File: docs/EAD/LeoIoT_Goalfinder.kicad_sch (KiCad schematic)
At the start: 16 parts, among them J1 USB_B_Micro_Breakout, J1e1 Conn_01x02_Pin, J2 LED Strip, J3 GAIN, Q1 IRFZ44N, U1 ESP32_D1_mini, U2 VL53L0X_Breakout, U3 MAX98357A_Breakout, U4 SW420_Breakout, U5 LIS3DH_Breakout

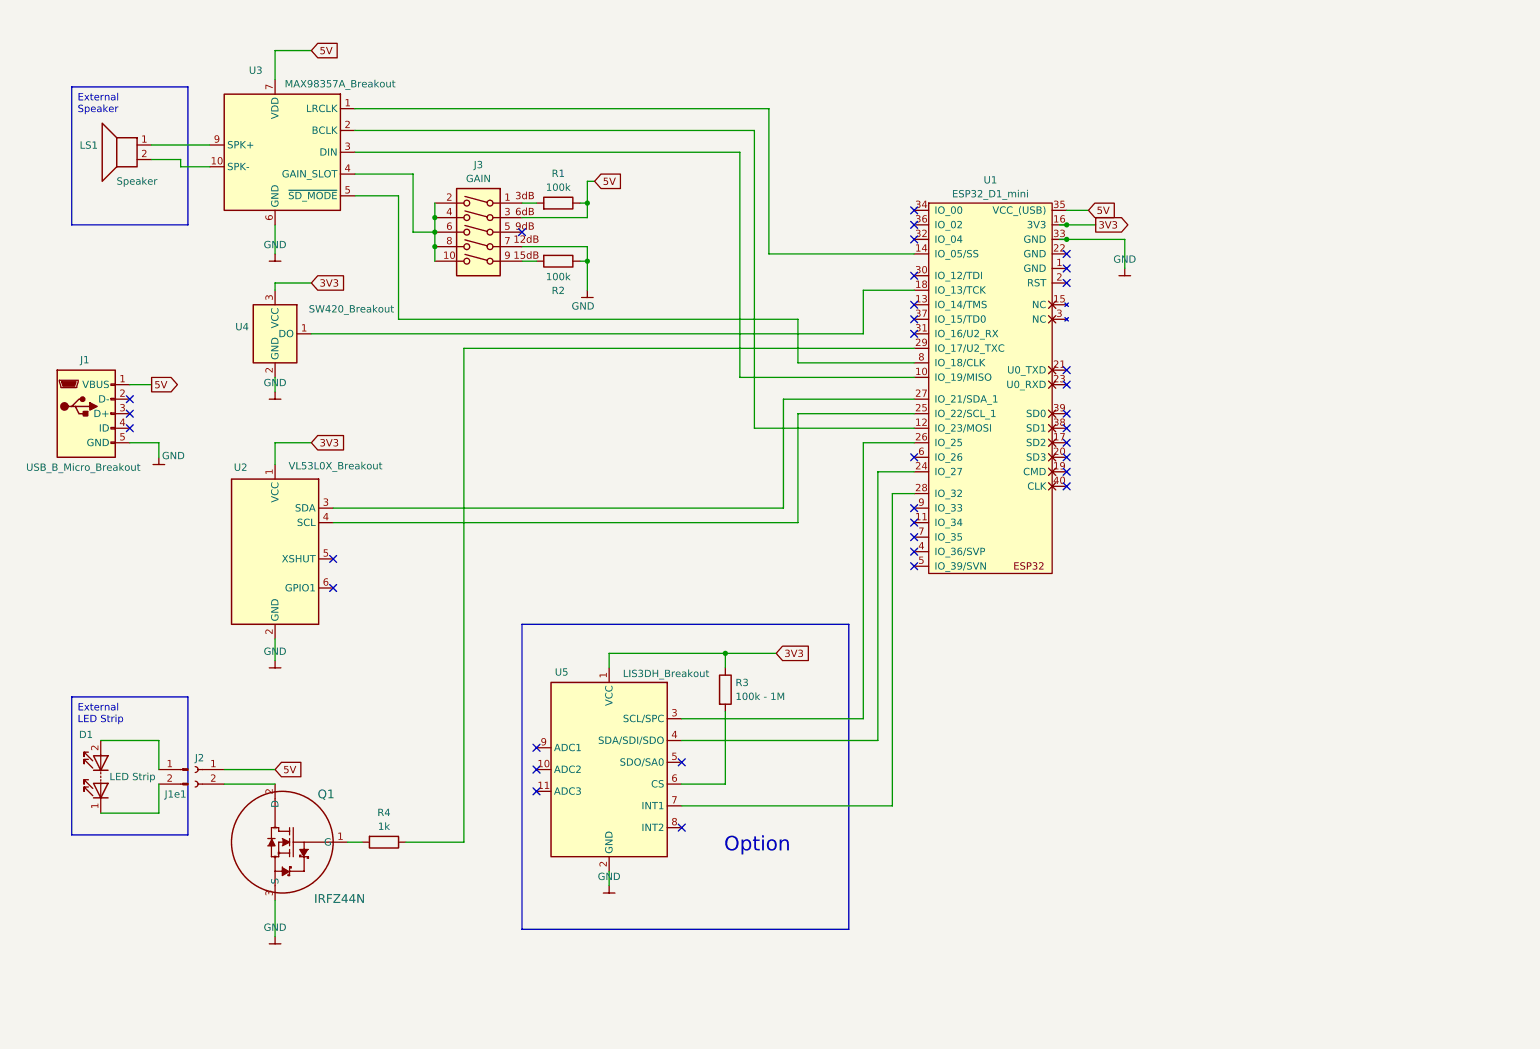
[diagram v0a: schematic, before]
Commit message: added power support capacities, updated schematic and PCB to r1.1
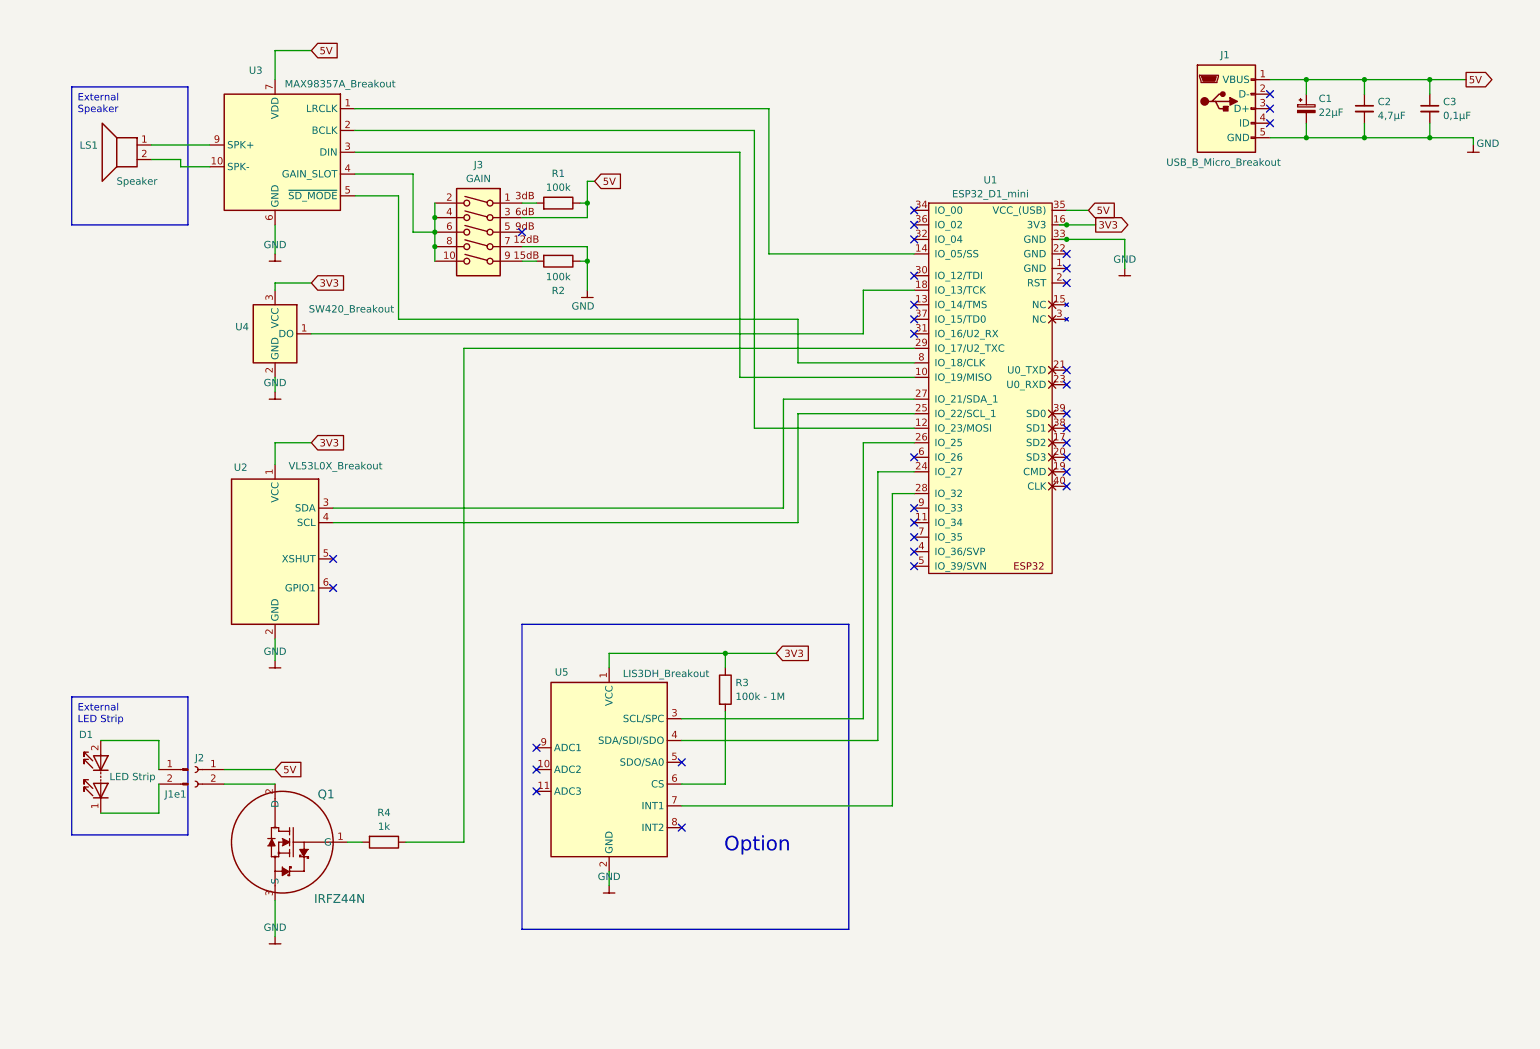
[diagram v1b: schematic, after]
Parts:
- added C1: 22µF, Capacitor_THT:CP_Radial_D5.0mm_P2.00mm, symbol Device:C_Polarized_Small
- added C2: 4,7µF, Capacitor_THT:CP_Radial_D5.0mm_P2.00mm, symbol Device:C_Small
- added C3: 0,1µF, Capacitor_THT:C_Rect_L13.0mm_W4.0mm_P10.00mm_FKS3_FKP3_MKS4, symbol Device:C_Small
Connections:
- net 5V: now also C1.1, C2.1, C3.1
- net GND: now also C1.2, C2.2, C3.2
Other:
- moved on the sheet: J1

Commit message: improved HW: - added capacitors for each breakout board - made GND lines wider and added GND shield areas - added HW revision 01.02 added technical drawings for case factoring
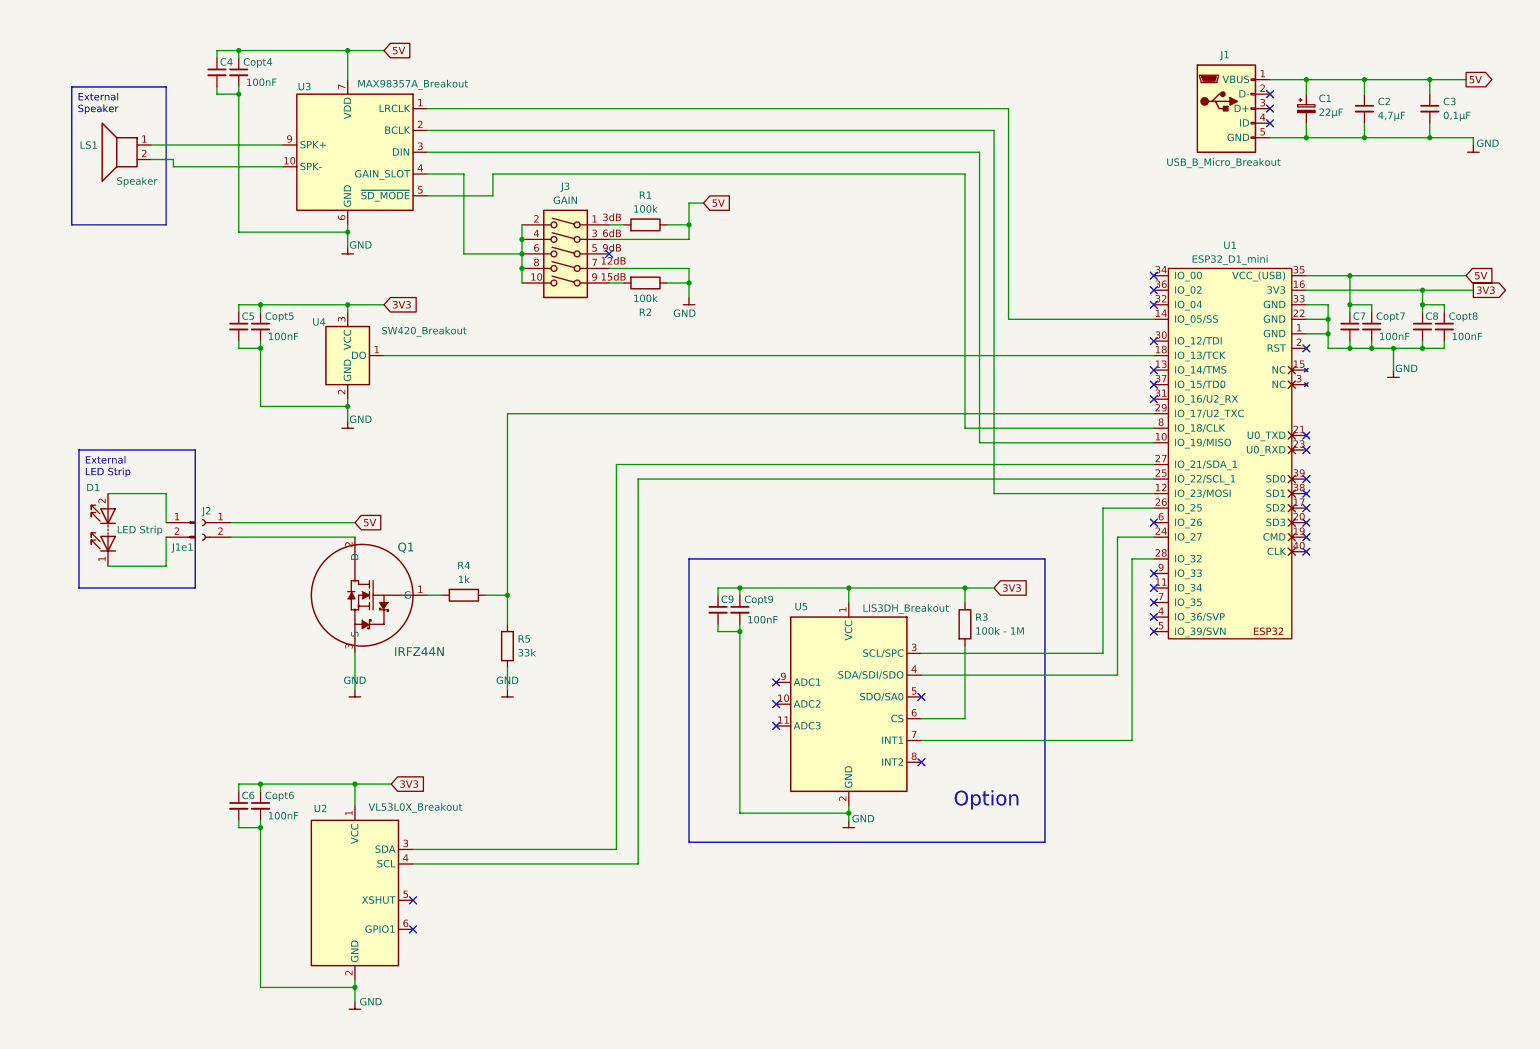
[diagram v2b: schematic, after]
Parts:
- added C4, C5, C6, C7, C8, C9: 100nF, Capacitor_SMD:C_0805_2012Metric_Pad1.18x1.45mm_HandSolder, symbol Device:C_Small
- added Copt4, Copt5, Copt6, Copt7, Copt8, Copt9: 100nF, Capacitor_THT:C_Disc_D5.0mm_W2.5mm_P2.50mm, symbol Device:C_Small
- added R5: 33k, Resistor_THT:R_Axial_DIN0309_L9.0mm_D3.2mm_P12.70mm_Horizontal, symbol Device:R
- R3, U5: now left out of the parts list
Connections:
- net 3V3: now also C5.1, C6.1, C8.1, C9.1, Copt5.1, Copt6.1, Copt8.1, Copt9.1
- net 5V: now also C4.1, C7.1, Copt4.1, Copt7.1
- net GND: now also U1.1 (GND), U1.22 (GND), C4.2, C5.2, C6.2, C7.2, C8.2, C9.2, Copt4.2, Copt5.2, Copt6.2, Copt7.2, Copt8.2, Copt9.2, R5.2
- net at R4.1, U1.29 (IO_17/U2_TXC): now also R5.1
- no-connect marks 35 -> 33
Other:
- moved on the sheet: D1, J1e1, J2, J3, Q1, R1, R2, R3, R4, U1, U2, U3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

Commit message: Refined design and PCB layout and added BOM - added SMD resistors - shaped PCB prints
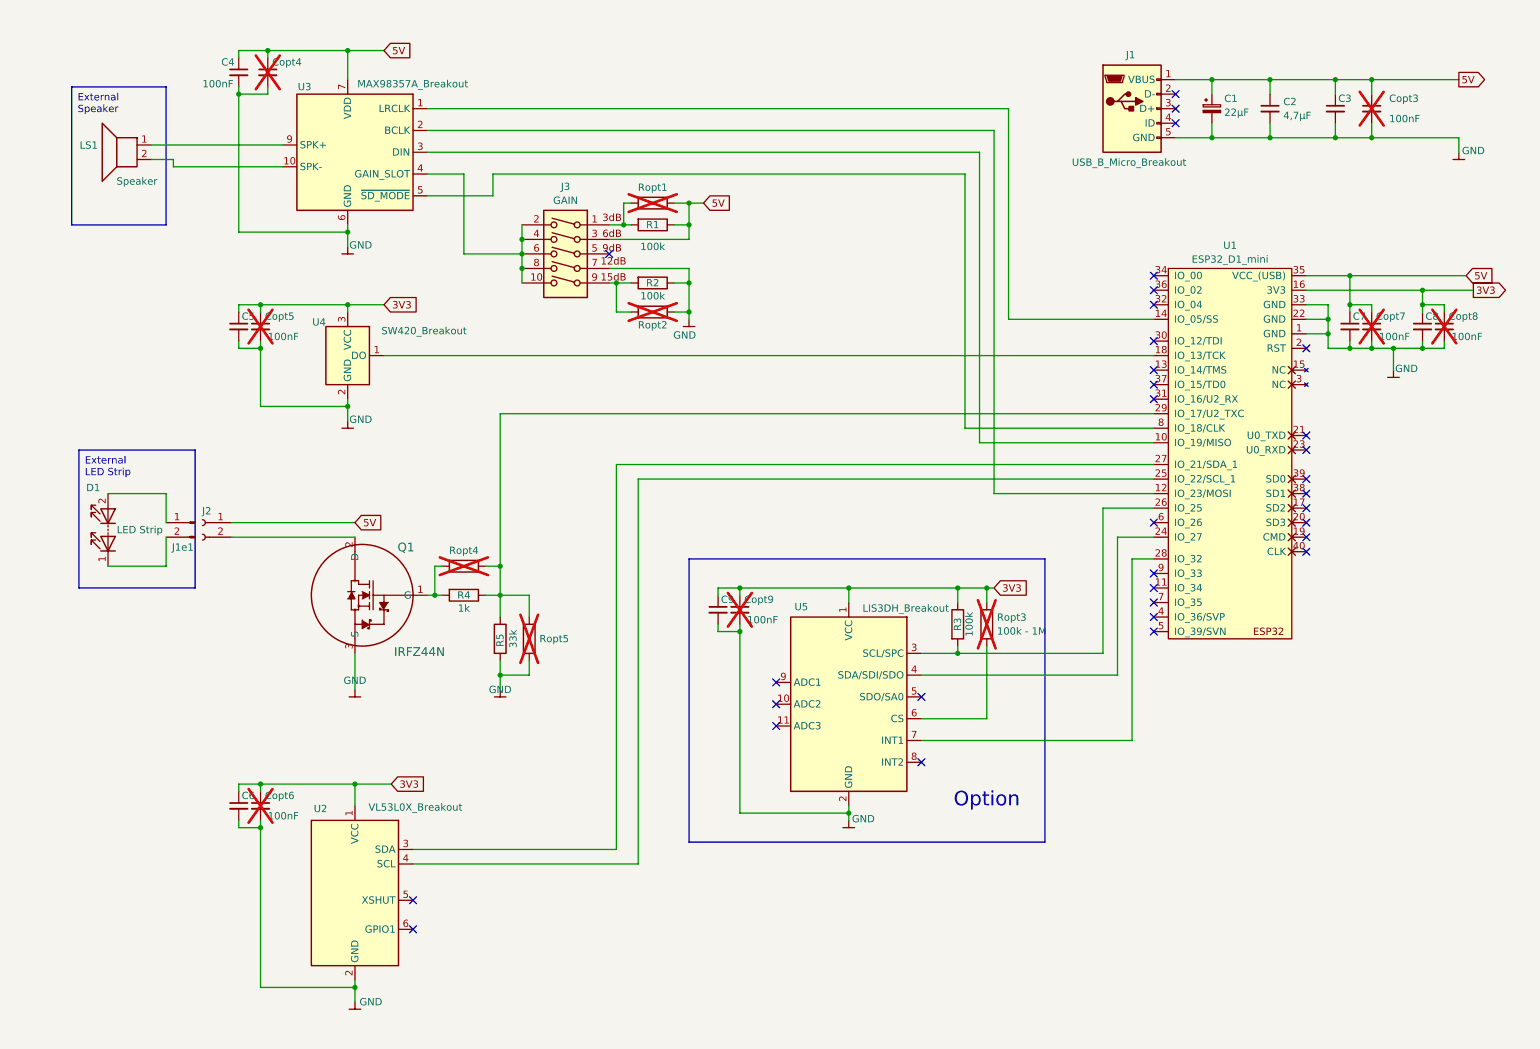
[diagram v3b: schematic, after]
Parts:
- added C3: 100nF, Capacitor_SMD:C_0805_2012Metric_Pad1.18x1.45mm_HandSolder, symbol Device:C_Small
- added R1, R2, R3: 100k, Resistor_SMD:R_0805_2012Metric_Pad1.20x1.40mm_HandSolder, symbol Device:R
- added R4: 1k, Resistor_SMD:R_0805_2012Metric_Pad1.20x1.40mm_HandSolder, symbol Device:R
- added R5: 33k, Resistor_SMD:R_0805_2012Metric_Pad1.20x1.40mm_HandSolder, symbol Device:R
- Copt3: renamed from C3; value 0,1µF -> 100nF; footprint Capacitor_THT:C_Rect_L13.0mm_W4.0mm_P10.00mm_FKS3_FKP3_MKS4 -> Capacitor_THT:C_Disc_D5.0mm_W2.5mm_P2.50mm; now not fitted
- Copt4, Copt5, Copt6, Copt7, Copt8, Copt9: now not fitted
- J1e1: now left out of the parts list
- Ropt1: renamed from R1; now not fitted
- Ropt2: renamed from R2; now not fitted
- Ropt3: renamed from R3; now not fitted
- Ropt4: renamed from R4; now not fitted
- Ropt5: renamed from R5; now not fitted
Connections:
- net 3V3: now also R3.1
- net 5V: now also C3.1, R1.1
- net GND: now also C3.2, R2.1, R5.2
- net at Ropt4.1, Ropt5.1, U1.29 (IO_17/U2_TXC): now also R4.1, R5.1
- net at Q1.1 (G), Ropt4.2: now also R4.2
- net at U1.26 (IO_25), U5.3 (SCL/SPC): now also R3.2
- net at J3.9, Ropt2.2: now also R2.2
- net at J3.1, Ropt1.2: now also R1.2
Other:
- moved on the sheet: C1, C2, C4, J1
